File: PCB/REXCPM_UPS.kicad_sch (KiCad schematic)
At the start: 7 parts, among them J1 Model_100_System_BUS, J2 Conn_01x03_Pin, U1 7402

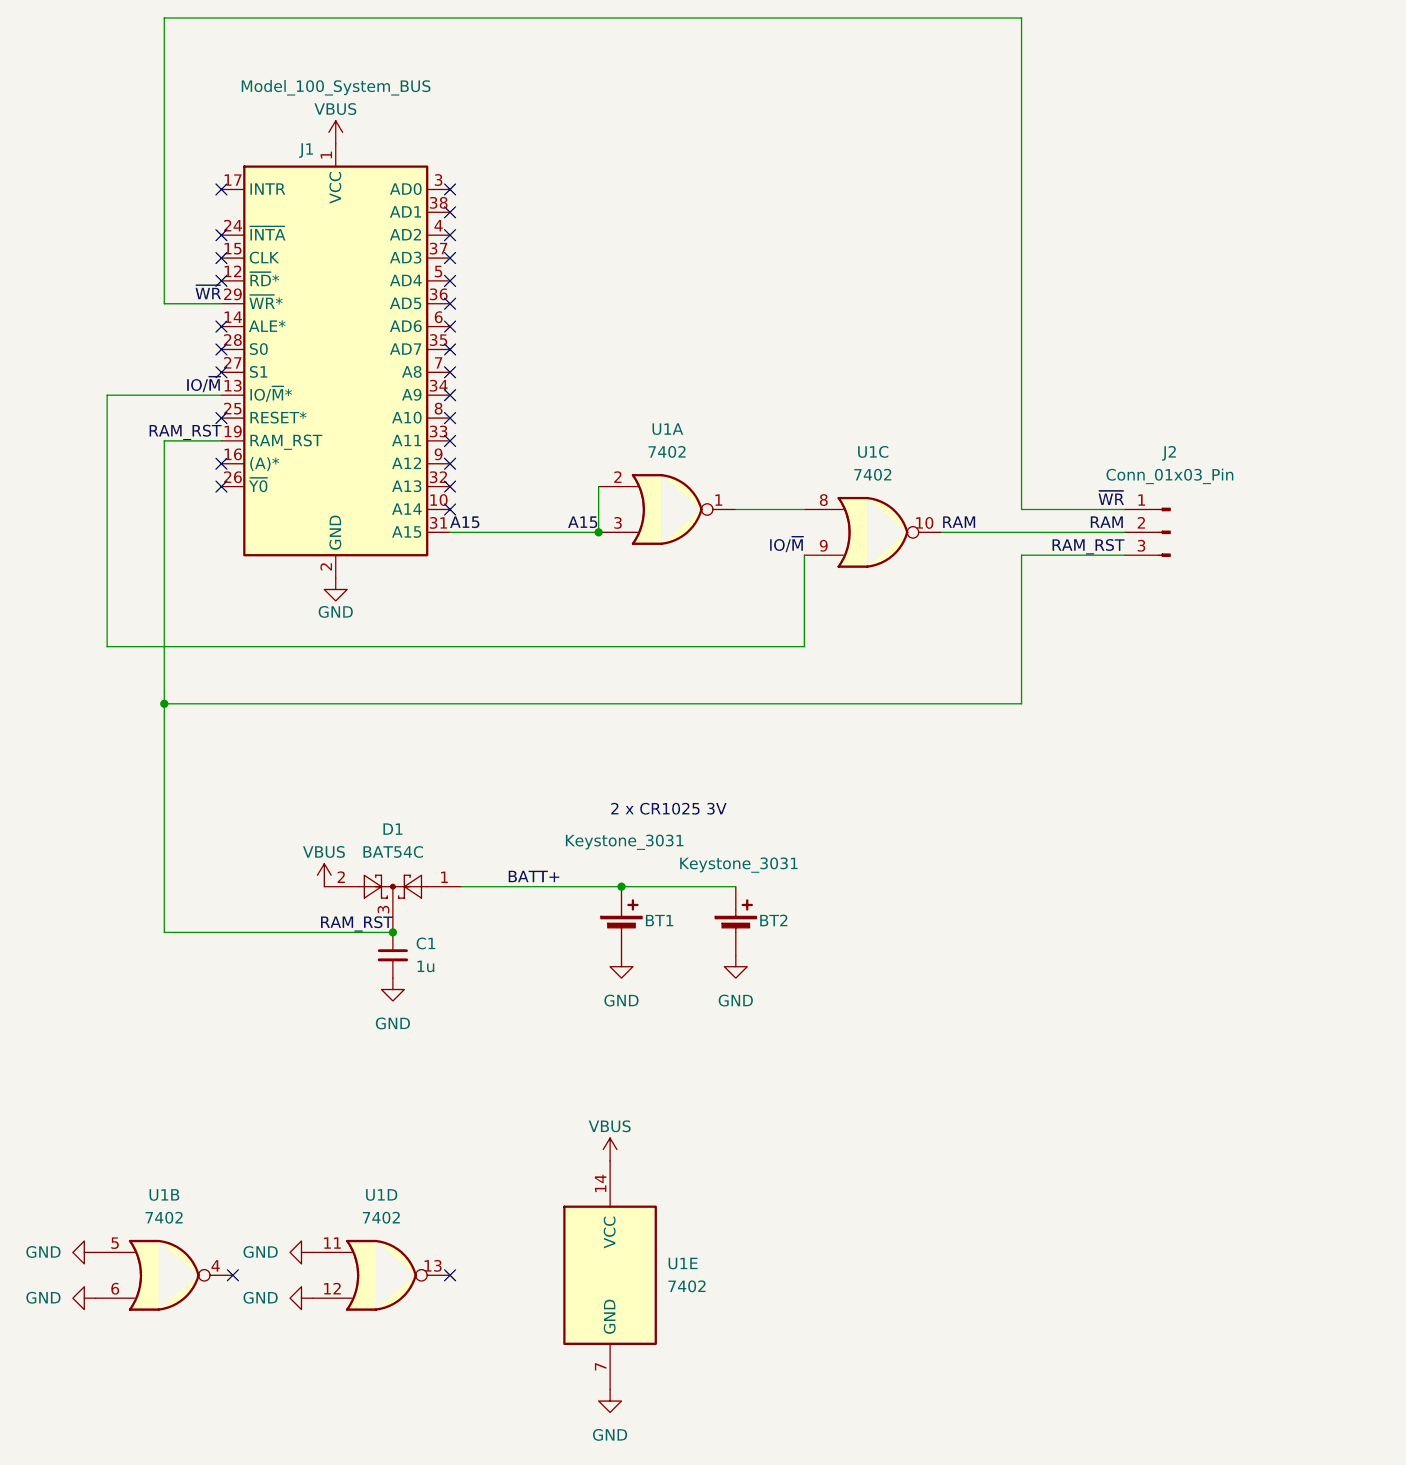
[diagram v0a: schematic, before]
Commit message: replace 7402 with 742g02
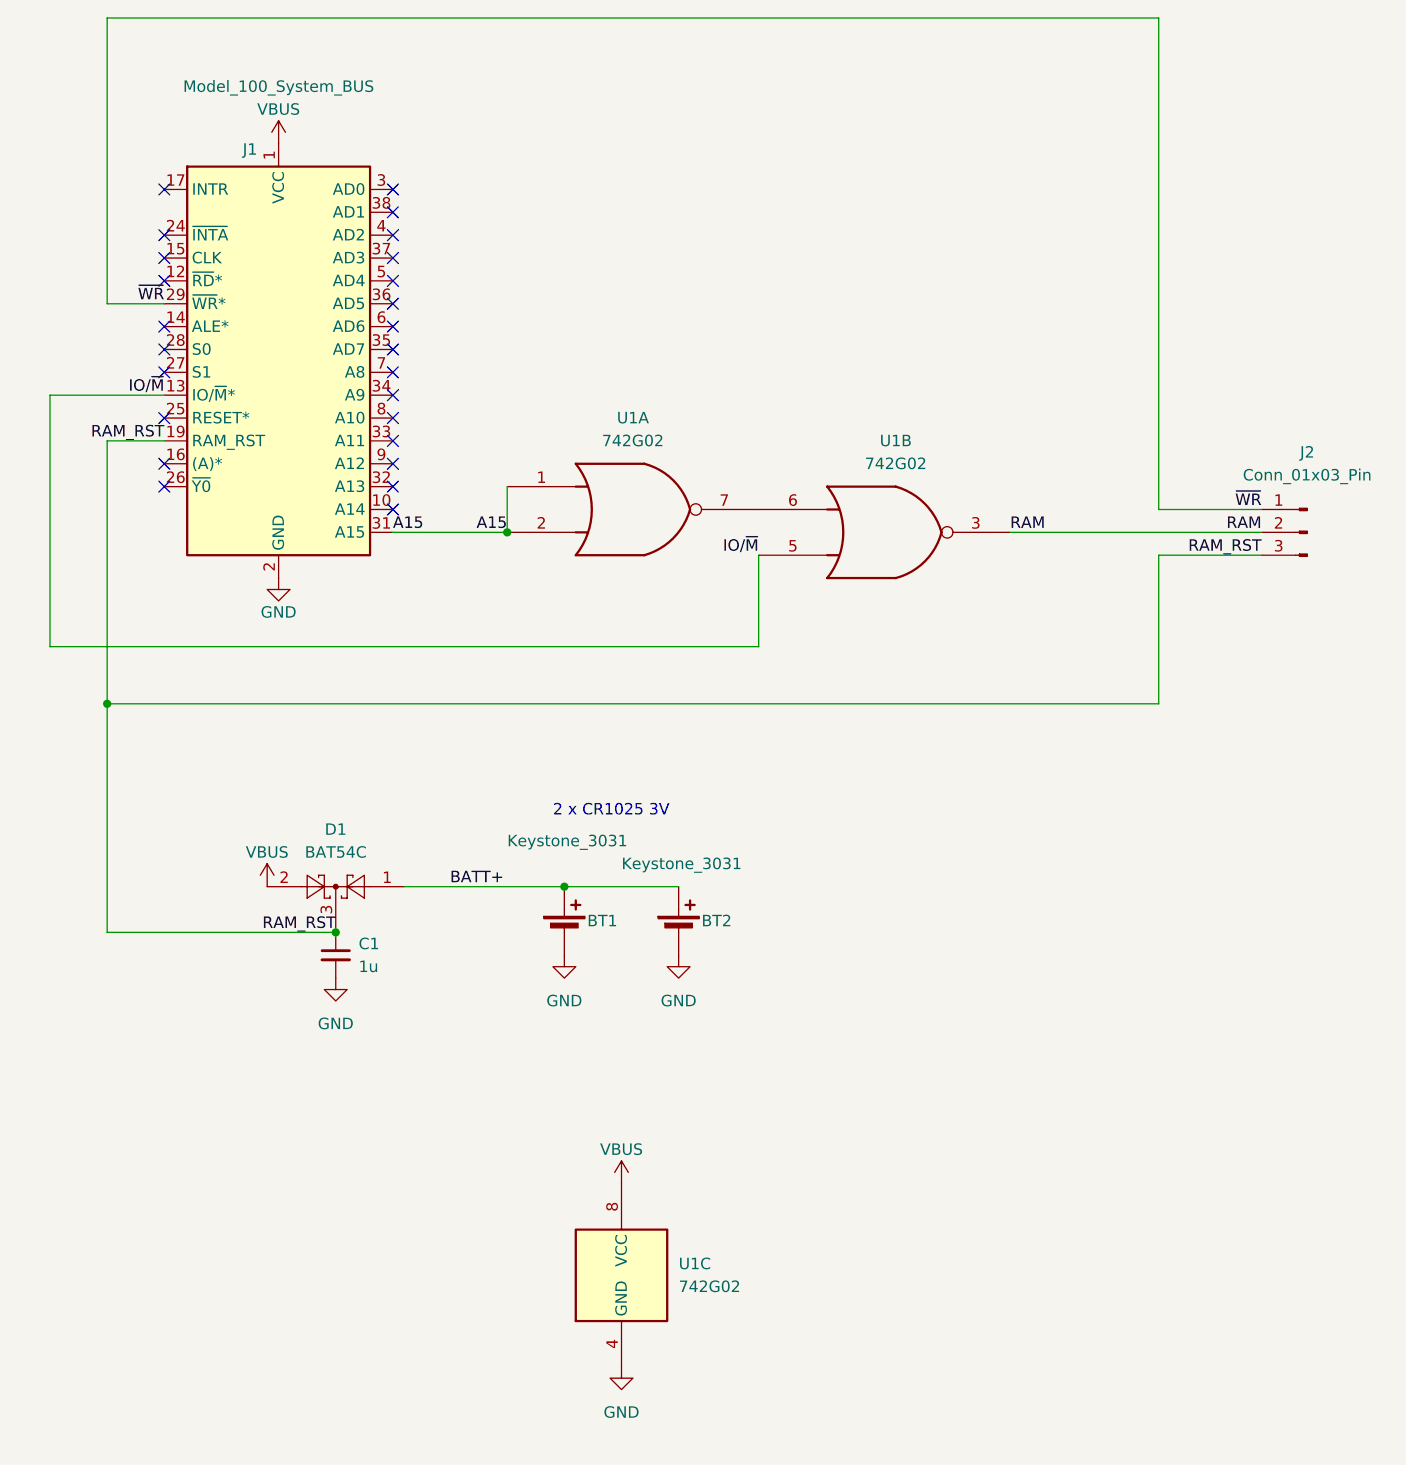
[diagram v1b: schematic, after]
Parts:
- removed U1: 7402, 000_LOCAL:TSSOP-14_4.4x5mm_P0.65mm, symbol 000_LOCAL:7402
- added U1: 742G02, 000_LOCAL:TSSOP-8_3x3mm_P0.65mm, symbol 000_LOCAL:742G02
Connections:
- net A15: now also U1.1, U1.2
- net GND: now also U1.4 (GND)
- net IO/~{M}: now also U1.5
- net RAM: now also U1.3
- net VBUS: now also U1.8 (VCC)
- new net: U1.6, U1.7
- no-connect marks 27 -> 25
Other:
- moved on the sheet: BT1, BT2, C1, D1, J1, J2
